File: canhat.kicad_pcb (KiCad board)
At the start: 2 copper layers, 65 x 30 mm, 27 parts, among them J1 Raspberry_Pi_2_3, J2 CAN In / Out, J3 5V, U1 MCP2515-xSO, U2 SN65HVD234, U3 AT24C32-SSHM, Y1 16MHz

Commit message: Redid layout to shorten long traces
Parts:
- J2: value CAN In / Out -> CAN In/Out/GND; footprint TerminalBlock_TE-Connectivity:TerminalBlock_TE_282834-4_1x04_P2.54mm_Horizontal -> TerminalBlock_TE-Connectivity:TerminalBlock_TE_282834-6_1x06_P2.54mm_Horizontal
- moved J3 57.0 mm to (44.0, 65.5), turned to 90 degrees
- moved C5 46.0 mm to (54.0, 65.5), turned to 0 degrees
- moved OSHW1 38.2 mm to (91.0, 72.0)
- moved R5 28.5 mm to (77.8, 77.5), turned to 270 degrees
- moved C6 25.0 mm to (75.8, 76.5), turned to 270 degrees
- moved J2 21.0 mm to (64.0, 76.0), turned to 180 degrees
- moved C2 20.7 mm to (81.0, 69.0), turned to 90 degrees
- moved U2 19.0 mm to (71.0, 76.5)
- moved Y1 17.7 mm to (85.0, 67.0), turned to 90 degrees
- moved R3 16.2 mm to (99.0, 66.5), turned to 180 degrees
- moved R4 14.1 mm to (99.0, 64.5), turned to 180 degrees
- moved R2 12.6 mm to (99.0, 62.5), turned to 180 degrees
- moved JP1 11.4 mm to (99.0, 59.0), turned to 90 degrees
- moved R1 10.0 mm to (68.5, 58.0), turned to 180 degrees
- moved C1 9.99 mm to (81.0, 65.0)
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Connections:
- J2 pad 1: /CAN_P -> GND
- J2 pad 2: /CAN_N -> /CAN_P
- J2 pad 4: /CAN_P -> /CAN_N
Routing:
- net +3V3: track 97.8 -> 6.18 mm
- net +5V: track 120.8 -> 35.4 mm
- net /RX: track 17.7 -> 6.86 mm
- net /SCK: track 17.0 -> 6.87 mm
- net /MOSI: track 15.7 -> 6.76 mm
- net /ID_SD: track 13.9 -> 22.3 mm
- net /~INT: track 24.4 -> 18.1 mm
- net /ID_SC: track 17.0 -> 23.3 mm, vias 1 -> 0
- net Net-(R5-Pad2): track 4.04 -> 9.98 mm
- net /MISO: track 12.3 -> 6.87 mm, vias 1 -> 0
- net Net-(C2-Pad2): track 17.5 -> 12.5 mm
- net Net-(C1-Pad1): track 18.8 -> 14.6 mm
- net /CAN_N: track 17.8 -> 21.8 mm
- net GND: track 20.7 -> 24.3 mm, vias 11 -> 10
- net /CAN_P: track 19.0 -> 22.4 mm
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- added copper zone on F.Cu, net +3V3
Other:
- board text added: "V3 RasPi CAN HAT © 2019 onitake"
- board text added: "⏚ H↓L L↑H ⏚"
- board text removed: "H OUT L IN H"
- board text removed: "V2 RasPi CAN HAT © 2019 onitake"

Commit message: Small optimizations
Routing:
- net /~CS: track 14.4 -> 15.4 mm
- net /MISO: track 6.87 -> 6.90 mm, vias 0 -> 1
- net /MOSI: vias 1 -> 0
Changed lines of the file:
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@@
     (thickness 1.6)
     (drawings 13)
-    (tracks 170)
+    (tracks 169)
     (zones 0)
     (modules 27)
@@
     (tags "resistor handsolder")
     (attr smd)
-    (fp_text reference R5 (at -3.025 0 90) (layer F.SilkS)
+    (fp_text reference R5 (at -3.375 -0.2 180) (layer F.SilkS)
       (effects (font (size 1 1) (thickness 0.15)))
     )
@@
   (segment (start 85.24 51) (end 86.47 52.23) (width 0.25) (layer F.Cu) (net 4))
   (segment (start 80.880998 51) (end 85.24 51) (width 0.25) (layer F.Cu) (net 4))
-  (segment (start 76.31 58.06) (end 76.31 54.77) (width 0.25) (layer F.Cu) (net 5))
-  (segment (start 74.27 60.8) (end 74.27 60.1) (width 0.25) (layer F.Cu) (net 5))
-  (segment (start 74.27 60.1) (end 76.31 58.06) (width 0.25) (layer F.Cu) (net 5))
-  (via (at 73 57.1) (size 0.8) (drill 0.4) (layers F.Cu B.Cu) (net 6))
-  (segment (start 73 60.8) (end 73 57.1) (width 0.25) (layer F.Cu) (net 6))
-  (segment (start 71.23 55.33) (end 71.23 54.77) (width 0.25) (layer B.Cu) (net 6))
-  (segment (start 73 57.1) (end 71.23 55.33) (width 0.25) (layer B.Cu) (net 6))
-  (segment (start 71.73 60.8) (end 71.73 56.81) (width 0.25) (layer F.Cu) (net 7))
-  (segment (start 71.73 56.81) (end 72.920001 55.619999) (width 0.25) (layer F.Cu) (net 7))
-  (segment (start 72.920001 55.619999) (end 73.77 54.77) (width 0.25) (layer F.Cu) (net 7))
+  (segment (start 74.27 56.81) (end 74.27 60.8) (width 0.25) (layer F.Cu) (net 5))
+  (segment (start 76.31 54.77) (end 74.27 56.81) (width 0.25) (layer F.Cu) (net 5))
+  (segment (start 73 56.54) (end 71.23 54.77) (width 0.25) (layer F.Cu) (net 6))
+  (segment (start 73 60.8) (end 73 56.54) (width 0.25) (layer F.Cu) (net 6))
+  (via (at 71.7 59.1) (size 0.8) (drill 0.4) (layers F.Cu B.Cu) (net 7))
+  (segment (start 71.73 60.8) (end 71.73 59.13) (width 0.25) (layer F.Cu) (net 7))
+  (segment (start 71.73 59.13) (end 71.7 59.1) (width 0.25) (layer F.Cu) (net 7))
+  (segment (start 73.77 57.03) (end 73.77 54.77) (width 0.25) (layer B.Cu) (net 7))
+  (segment (start 71.7 59.1) (end 73.77 57.03) (width 0.25) (layer B.Cu) (net 7))
   (via (at 70.5 62.5) (size 0.8) (drill 0.4) (layers F.Cu B.Cu) (net 8))
   (segment (start 70.46 60.8) (end 70.46 62.46) (width 0.25) (layer F.Cu) (net 8))
   (segment (start 70.46 62.46) (end 70.5 62.5) (width 0.25) (layer F.Cu) (net 8))
-  (segment (start 75.134999 53.405001) (end 75.460001 53.079999) (width 0.25) (layer B.Cu) (net 8))
-  (segment (start 75.134999 57.865001) (end 75.134999 53.405001) (width 0.25) (layer B.Cu) (net 8))
-  (segment (start 75.460001 53.079999) (end 76.31 52.23) (width 0.25) (layer B.Cu) (net 8))
-  (segment (start 70.5 62.5) (end 75.134999 57.865001) (width 0.25) (layer B.Cu) (net 8))
+  (segment (start 77.159999 53.079999) (end 76.31 52.23) (width 0.25) (layer B.Cu) (net 8))
+  (segment (start 77.485001 53.405001) (end 77.159999 53.079999) (width 0.25) (layer B.Cu) (net 8))
+  (segment (start 77.485001 55.514999) (end 77.485001 53.405001) (width 0.25) (layer B.Cu) (net 8))
+  (segment (start 70.5 62.5) (end 77.485001 55.514999) (width 0.25) (layer B.Cu) (net 8))
   (segment (start 69.55 59.19) (end 69.55 58) (width 0.25) (layer F.Cu) (net 9))
   (segment (start 69.19 60.8) (end 69.19 59.55) (width 0.25) (layer F.Cu) (net 9))

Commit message: Cosmetics
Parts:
- moved C7 0.30 mm to (93.7, 59.8)
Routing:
- net /~INT: track 18.1 -> 15.9 mm, vias 0 -> 1
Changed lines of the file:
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@@
     (thickness 1.6)
     (drawings 13)
-    (tracks 169)
+    (tracks 173)
     (zones 0)
     (modules 27)
@@
   )
   (module Capacitor_SMD:C_0805_2012Metric_Pad1.15x1.40mm_HandSolder (layer F.Cu)
-    (at 93.475 60 180)
+    (at 93.7 59.8 180)
     (descr "Capacitor SMD 0805 (2012 Metric), square (rectangular) end terminal, IPC_7351 nominal with elongated pad for handsoldering. (Body size source: https://docs.google.com/spreadsheets/d/1BsfQQcO9C6DZCsRaXUlFlo91Tg2WpOkGARC1WS5S8t0/edit?usp=sharing), generated with kicad-footprint-generator")
     (tags "capacitor handsolder")
@@
   (segment (start 78.08 71.88) (end 78.1 71.9) (width 0.25) (layer F.Cu) (net 3))
   (segment (start 89.3 65.905) (end 89.3 62.095) (width 0.25) (layer F.Cu) (net 3))
-  (via (at 92.4 58.6) (size 0.8) (drill 0.4) (layers F.Cu B.Cu) (net 3))
-  (segment (start 92.45 60) (end 92.45 58.65) (width 0.25) (layer F.Cu) (net 3))
-  (segment (start 92.45 58.65) (end 92.4 58.6) (width 0.25) (layer F.Cu) (net 3))
   (via (at 90.8 65.8) (size 0.8) (drill 0.4) (layers F.Cu B.Cu) (net 3))
   (segment (start 89.3 65.905) (end 90.695 65.905) (width 0.25) (layer F.Cu) (net 3))
@@
   (segment (start 72.335 77.135) (end 72.3 77.1) (width 0.25) (layer F.Cu) (net 3))
   (segment (start 73.7 77.135) (end 72.335 77.135) (width 0.25) (layer F.Cu) (net 3))
-  (segment (start 80.214999 51.665999) (end 80.880998 51) (width 0.25) (layer F.Cu) (net 4))
-  (segment (start 80.214999 55.425001) (end 80.214999 51.665999) (width 0.25) (layer F.Cu) (net 4))
+  (via (at 92.7 58.5) (size 0.8) (drill 0.4) (layers F.Cu B.Cu) (net 3))
+  (segment (start 92.675 59.8) (end 92.675 58.525) (width 0.25) (layer F.Cu) (net 3))
+  (segment (start 92.675 58.525) (end 92.7 58.5) (width 0.25) (layer F.Cu) (net 3))
   (segment (start 75.54 60.8) (end 75.54 60.1) (width 0.25) (layer F.Cu) (net 4))
-  (segment (start 75.54 60.1) (end 80.214999 55.425001) (width 0.25) (layer F.Cu) (net 4))
-  (segment (start 85.24 51) (end 86.47 52.23) (width 0.25) (layer F.Cu) (net 4))
-  (segment (start 80.880998 51) (end 85.24 51) (width 0.25) (layer F.Cu) (net 4))
+  (via (at 81.4 56.9) (size 0.8) (drill 0.4) (layers F.Cu B.Cu) (net 4))
+  (segment (start 78.2 57.44) (end 78.74 56.9) (width 0.25) (layer F.Cu) (net 4))
+  (segment (start 78.74 56.9) (end 81.4 56.9) (width 0.25) (layer F.Cu) (net 4))
+  (segment (start 75.54 60.1) (end 78.2 57.44) (width 0.25) (layer F.Cu) (net 4))
+  (segment (start 85.620001 53.079999) (end 86.47 52.23) (width 0.25) (layer B.Cu) (net 4))
+  (segment (start 85.294999 53.405001) (end 85.620001 53.079999) (width 0.25) (layer B.Cu) (net 4))
+  (segment (start 85.294999 55.144003) (end 85.294999 53.405001) (width 0.25) (layer B.Cu) (net 4))
+  (segment (start 83.539002 56.9) (end 85.294999 55.144003) (width 0.25) (layer B.Cu) (net 4))
+  (segment (start 81.4 56.9) (end 83.539002 56.9) (width 0.25) (layer B.Cu) (net 4))
   (segment (start 74.27 56.81) (end 74.27 60.8) (width 0.25) (layer F.Cu) (net 5))
   (segment (start 76.31 54.77) (end 74.27 56.81) (width 0.25) (layer F.Cu) (net 5))
@@
   (segment (start 69.19 60.8) (end 69.19 59.55) (width 0.25) (layer F.Cu) (net 9))
   (segment (start 69.19 59.55) (end 69.55 59.19) (width 0.25) (layer F.Cu) (net 9))
-  (segment (start 94.7 60.2) (end 94.5 60) (width 0.25) (layer F.Cu) (net 10))
-  (segment (start 94.7 62.095) (end 94.7 60.2) (width 0.25) (layer F.Cu) (net 10))
   (segment (start 100.05 66.5) (end 100.05 62.5) (width 0.25) (layer F.Cu) (net 10))
+  (segment (start 94.7 59.825) (end 94.725 59.8) (width 0.25) (layer F.Cu) (net 10))
+  (segment (start 94.7 62.095) (end 94.7 59.825) (width 0.25) (layer F.Cu) (net 10))
   (segment (start 97.405 65.905) (end 98 66.5) (width 0.25) (layer F.Cu) (net 11))
   (segment (start 94.7 65.905) (end 97.405 65.905) (width 0.25) (layer F.Cu) (net 11))

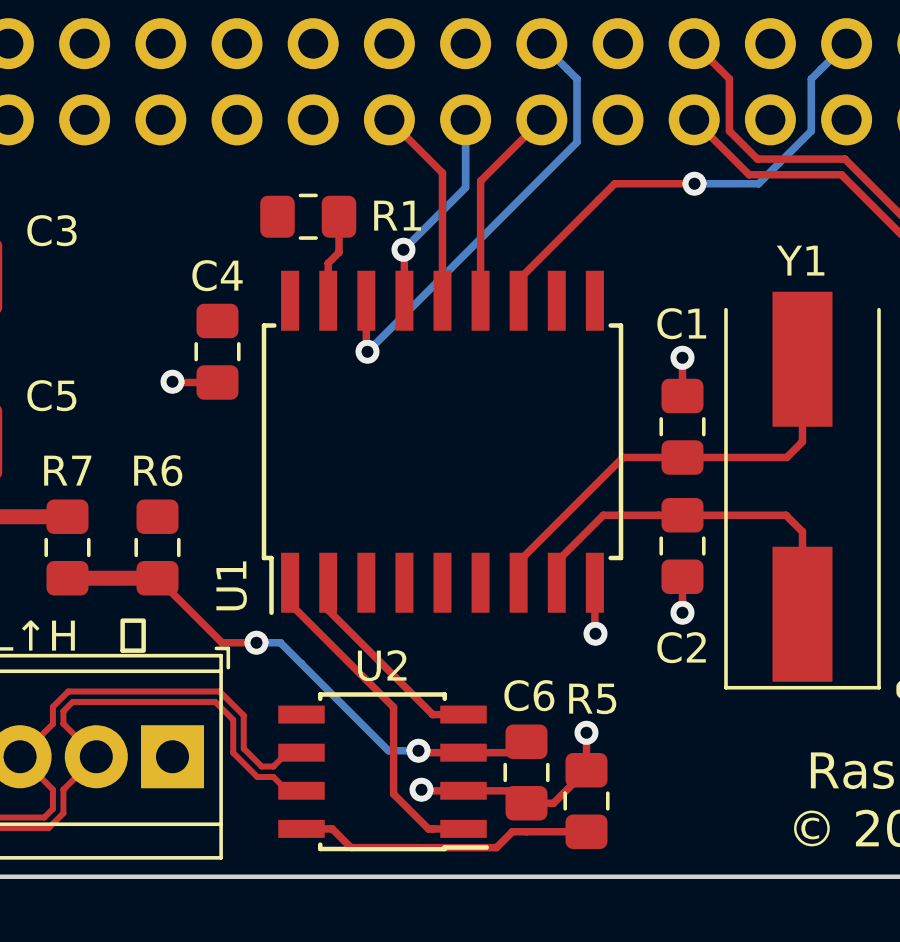
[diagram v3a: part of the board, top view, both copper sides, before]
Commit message: Added protective resistors between xceiver and controller
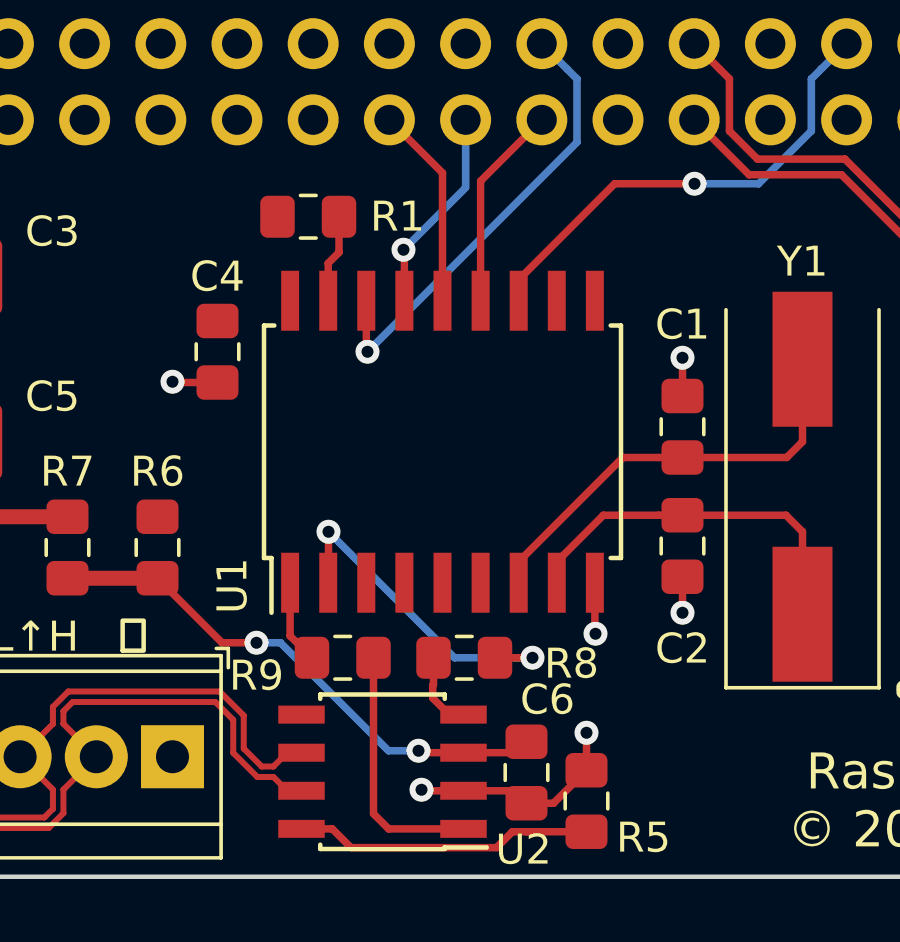
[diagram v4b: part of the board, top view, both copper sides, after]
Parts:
- added R8: 1k, Resistor_SMD:R_0805_2012Metric_Pad1.15x1.40mm_HandSolder, F.Cu at (73.7, 72.7)
- added R9: 1k, Resistor_SMD:R_0805_2012Metric_Pad1.15x1.40mm_HandSolder, F.Cu at (69.7, 72.7)
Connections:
- U1 pad 1: /TX -> Net-(R9-Pad1)
- U1 pad 2: /RX -> Net-(R8-Pad1)
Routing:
- net Net-(R8-Pad1): track 0.00 -> 11.5 mm, vias 0 -> 2
- net /RX: track 6.86 -> 2.61 mm
- net /TX: track 11.3 -> 8.41 mm
- net Net-(R9-Pad1): track 0.00 -> 2.80 mm

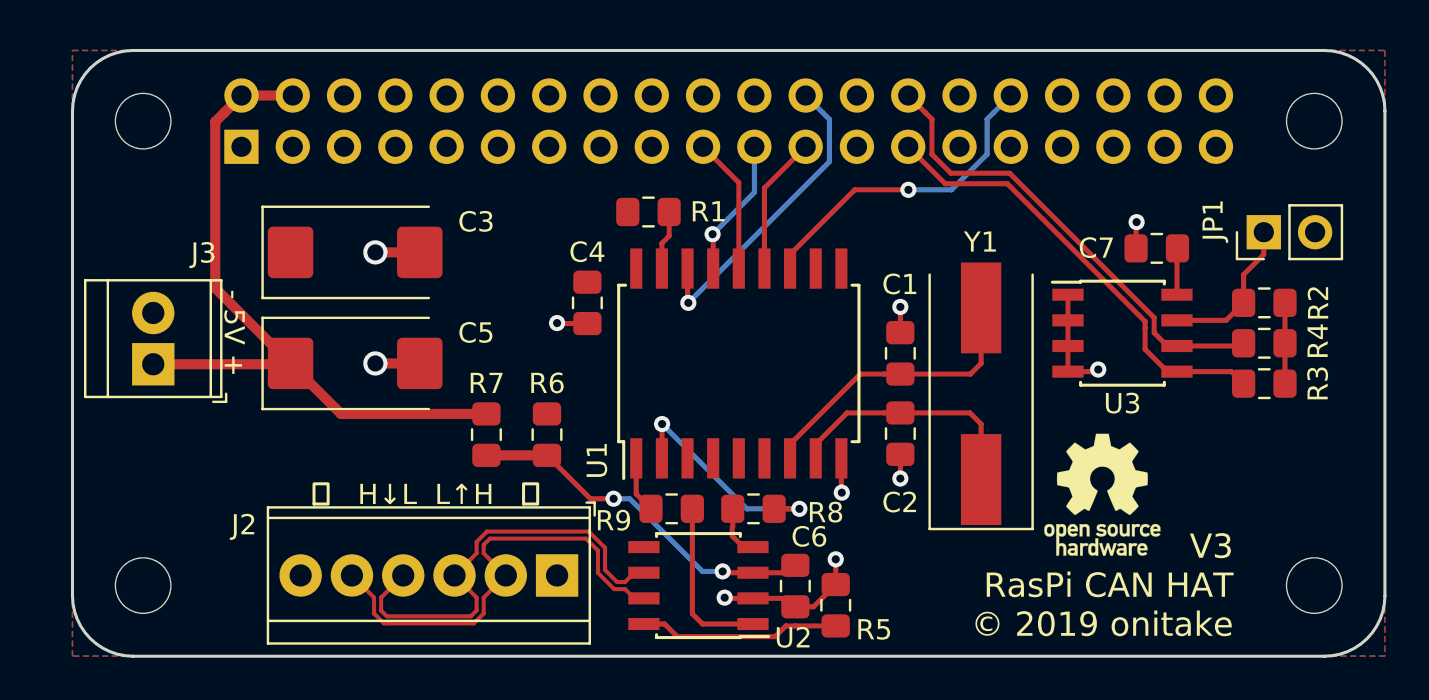
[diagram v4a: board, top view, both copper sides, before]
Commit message: Added 12V step-down power supply
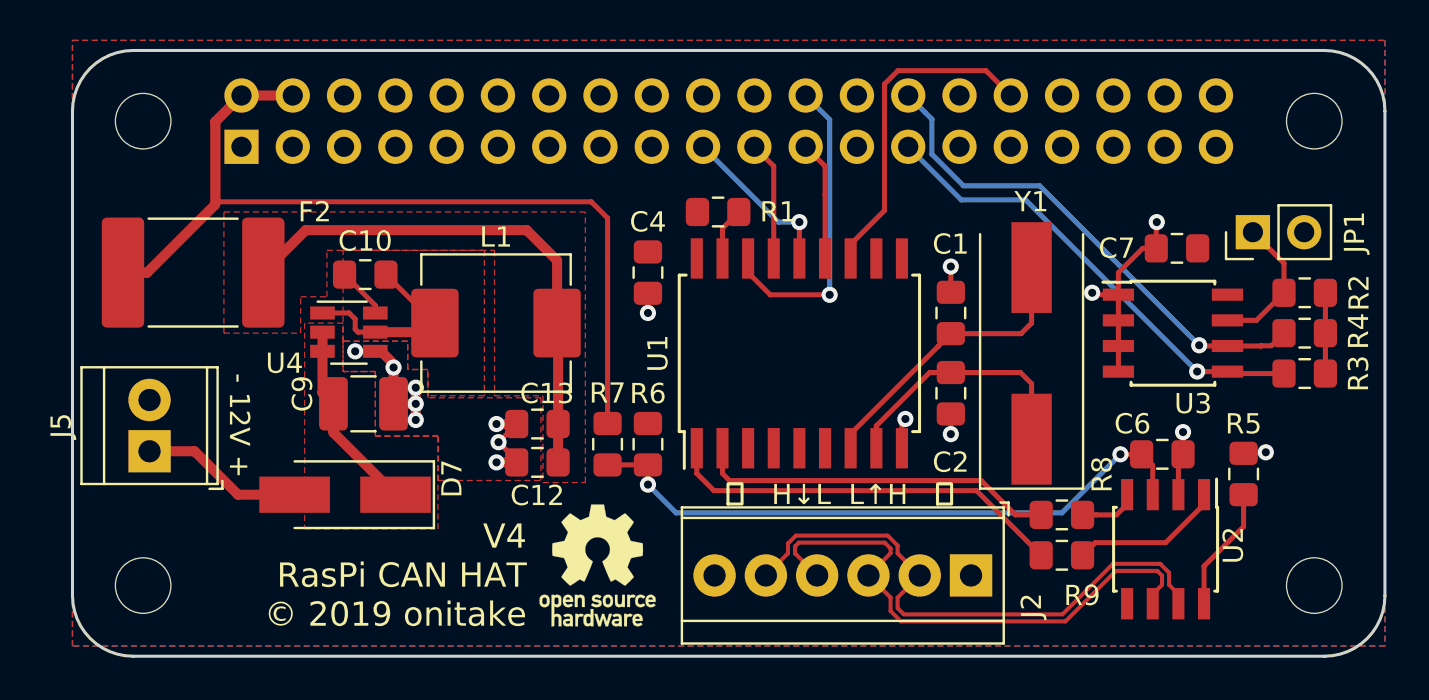
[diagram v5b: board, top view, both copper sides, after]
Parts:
- removed C3, C5: 10u, Capacitor_Tantalum_SMD:CP_EIA-7343-31_Kemet-D_Pad2.25x2.55mm_HandSolder
- removed J3: 5V, TerminalBlock_TE-Connectivity:TerminalBlock_TE_282834-2_1x02_P2.54mm_Horizontal
- added C10: 100n, Capacitor_SMD:C_0805_2012Metric_Pad1.15x1.40mm_HandSolder, F.Cu at (54.5, 61.1)
- added C12: 22u, Capacitor_SMD:C_0805_2012Metric_Pad1.15x1.40mm_HandSolder, F.Cu at (63.0, 70.4)
- added C13: 22u, Capacitor_SMD:C_0805_2012Metric_Pad1.15x1.40mm_HandSolder, F.Cu at (63.0, 68.5)
- added C9: 10u, Capacitor_SMD:C_1210_3225Metric_Pad1.42x2.65mm_HandSolder, F.Cu at (54.4, 67.5)
- added D7: D_Schottky, Diode_SMD:D_SMA_Handsoldering, F.Cu at (53.5, 72.0)
- added F2: 2920L200, Fuse:Fuse_2920_7451Metric_Pad2.10x5.45mm_HandSolder, F.Cu at (46.0, 61.0)
- added J5: 12V, TerminalBlock_TE-Connectivity:TerminalBlock_TE_282834-2_1x02_P2.54mm_Horizontal, F.Cu at (43.8, 69.8)
- added L1: 4.7u, Inductor_SMD:L_Abracon_ASPI-0630LR, F.Cu at (61.0, 63.5)
- added U4: AP63205, Package_TO_SOT_SMD:TSOT-23-6, F.Cu at (53.7, 64.0)
- moved OSHW1 25.2 mm to (66.0, 75.5)
- moved U2 23.2 mm to (94.1, 74.7), turned to 270 degrees
- moved R5 21.2 mm to (98.0, 71.0)
- moved J2 20.5 mm to (84.5, 76.0)
- moved R9 19.5 mm to (89.0, 75.0)
- moved C6 19.3 mm to (94.0, 70.0), turned to 0 degrees
- moved R8 15.3 mm to (89.0, 73.0), turned to 0 degrees
- moved R7 6.02 mm to (66.5, 69.5)
- moved R6 5.02 mm to (68.5, 69.5)
- moved R1 3.45 mm to (72.0, 58.0)
- moved C4 3.35 mm to (68.5, 61.0)
- moved C1 3.20 mm to (83.5, 63.0)
- moved C2 3.20 mm to (83.5, 67.0)
- moved Y1 3.20 mm to (87.5, 65.0)
- moved U1 3.04 mm to (76.0, 65.0)
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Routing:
- net Net-(C12-Pad1): track 0.00 -> 26.1 mm
- net Net-(R9-Pad1): track 2.80 -> 20.0 mm
- net +5V: track 35.4 -> 50.0 mm
- net VBUS: track 17.9 -> 31.4 mm
- net +12V: track 0.00 -> 12.6 mm
- net Net-(C10-Pad2): track 0.00 -> 9.87 mm
- net Net-(D7-Pad2): track 0.00 -> 8.08 mm
- net Net-(R8-Pad1): track 11.5 -> 17.9 mm, vias 2 -> 0
- net GND: track 24.1 -> 30.5 mm, vias 10 -> 16
- net /CAN_P: track 22.4 -> 28.4 mm
- net /CAN_N: track 21.8 -> 27.2 mm
- net Net-(R5-Pad2): track 9.98 -> 6.21 mm
- net Net-(C10-Pad1): track 0.00 -> 2.53 mm
- net +3V3: track 6.31 -> 4.04 mm
- net /ID_SC: track 23.3 -> 25.2 mm, vias 0 -> 1
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- added copper zone on F.Cu, net +12V
- added copper zone on F.Cu, net GND
- added copper zone on F.Cu, net Net-(C10-Pad2)
- added copper zone on F.Cu, net Net-(C12-Pad1)
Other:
- board text added: "- 12V +"
- board text added: "V4 RasPi CAN HAT © 2019 onitake"
- board text removed: "- 5V +"
- board text removed: "V3 RasPi CAN HAT © 2019 onitake"

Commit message: Removed obsolete PSU and added missing 3.3V cap
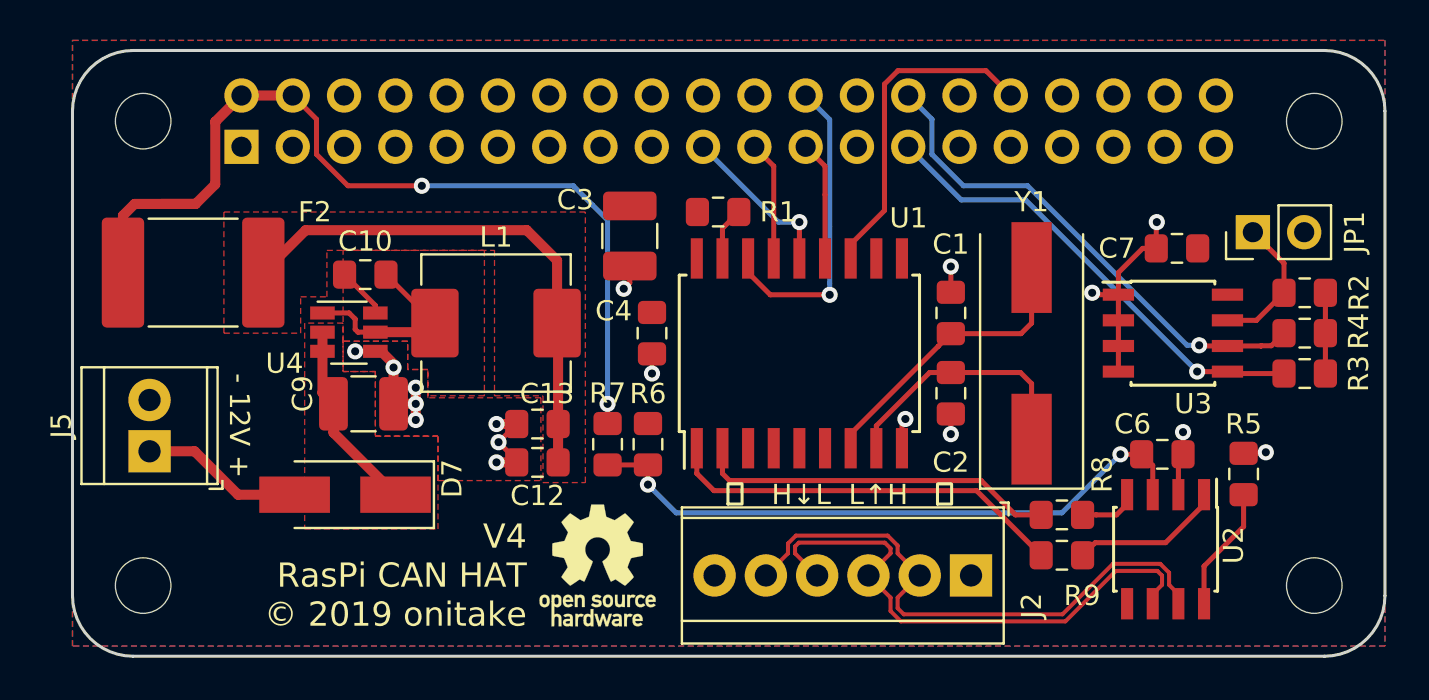
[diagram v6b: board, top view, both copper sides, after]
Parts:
- added C3: 10u, Capacitor_SMD:C_1210_3225Metric_Pad1.42x2.65mm_HandSolder, F.Cu at (67.6, 59.2)
- D7: value D_Schottky -> SS24
- moved C4 3.01 mm to (68.7, 64.0)
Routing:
- net +5V: track 50.0 -> 46.5 mm, vias 0 -> 2
- net GND: track 30.5 -> 31.7 mm, vias 16 -> 17
